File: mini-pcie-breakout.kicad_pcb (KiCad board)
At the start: 4 copper layers, 33 x 71.5 mm, 28 parts, among them J1 miniPCIe, J2 RX, J3 TX, J4 CLK, U1 AMS1117-1.5

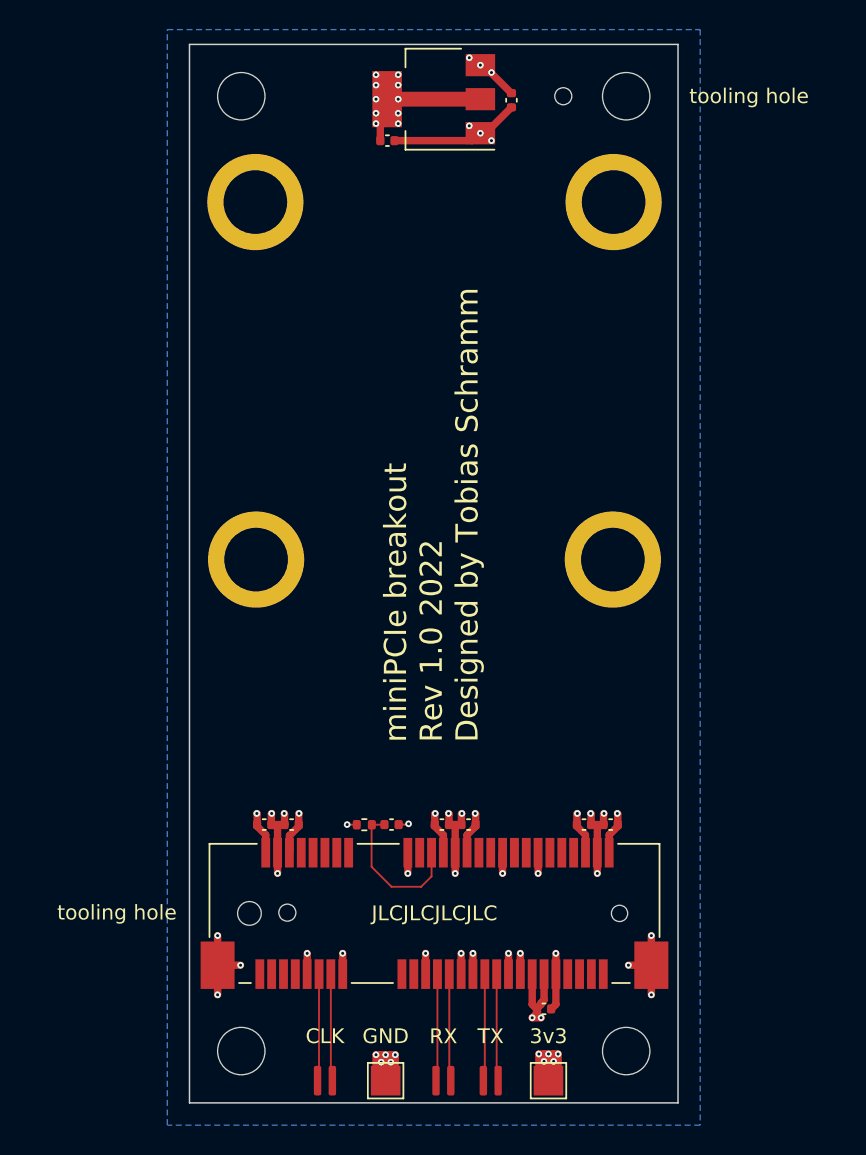
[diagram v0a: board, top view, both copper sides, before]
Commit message: Add half-size mini PCIe support
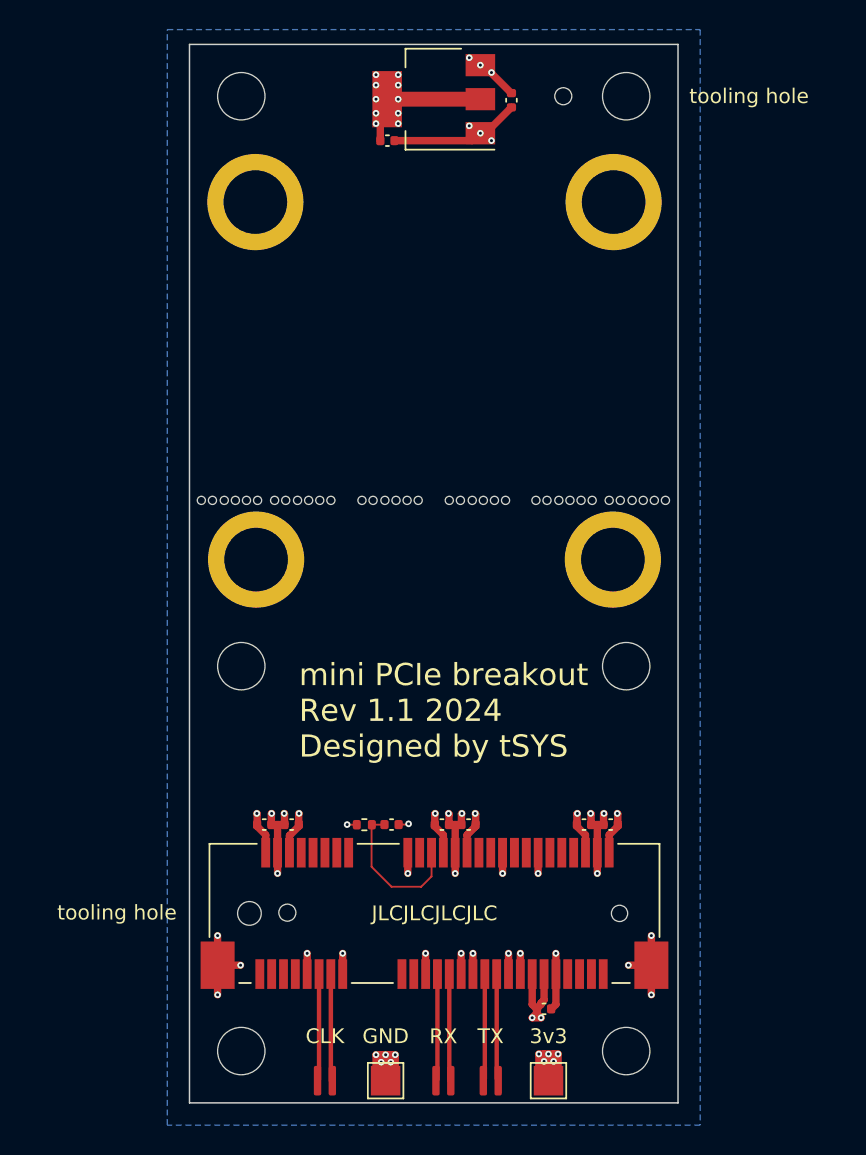
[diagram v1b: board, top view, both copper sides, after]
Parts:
- added H11: M3, MountingHole:MountingHole_3.2mm_M3, F.Cu at (47.0, 70.0)
- added H12: M3, MountingHole:MountingHole_3.2mm_M3, F.Cu at (73.0, 70.0)
- added REF**: MouseBites_JLCSMT, ToolingHole:MouseBites_JLCSMT, F.Cu at (46.2, 58.8)
- added REF**1: MouseBites_JLCSMT, ToolingHole:MouseBites_JLCSMT, F.Cu at (51.2, 58.8)
- added REF**2: MouseBites_JLCSMT, ToolingHole:MouseBites_JLCSMT, F.Cu at (57.1, 58.8)
- added REF**3: MouseBites_JLCSMT, ToolingHole:MouseBites_JLCSMT, F.Cu at (63.0, 58.8)
- added REF**4: MouseBites_JLCSMT, ToolingHole:MouseBites_JLCSMT, F.Cu at (68.8, 58.8)
- added REF**5: MouseBites_JLCSMT, ToolingHole:MouseBites_JLCSMT, F.Cu at (73.8, 58.8)
- H3, H4: value Standoff -> DNP
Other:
- board text added: "mini PCIe breakout Rev 1.1 2024 Designed by tSYS"
- board text removed: "miniPCIe breakout Rev 1.0 2022 Designed by Tobias Schramm"
